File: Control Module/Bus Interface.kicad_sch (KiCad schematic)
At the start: 5 parts, among them J2 Conn_01x22, J3 Conn_01x22, U11 74HC08, U12 74HC08, U13 74HC08

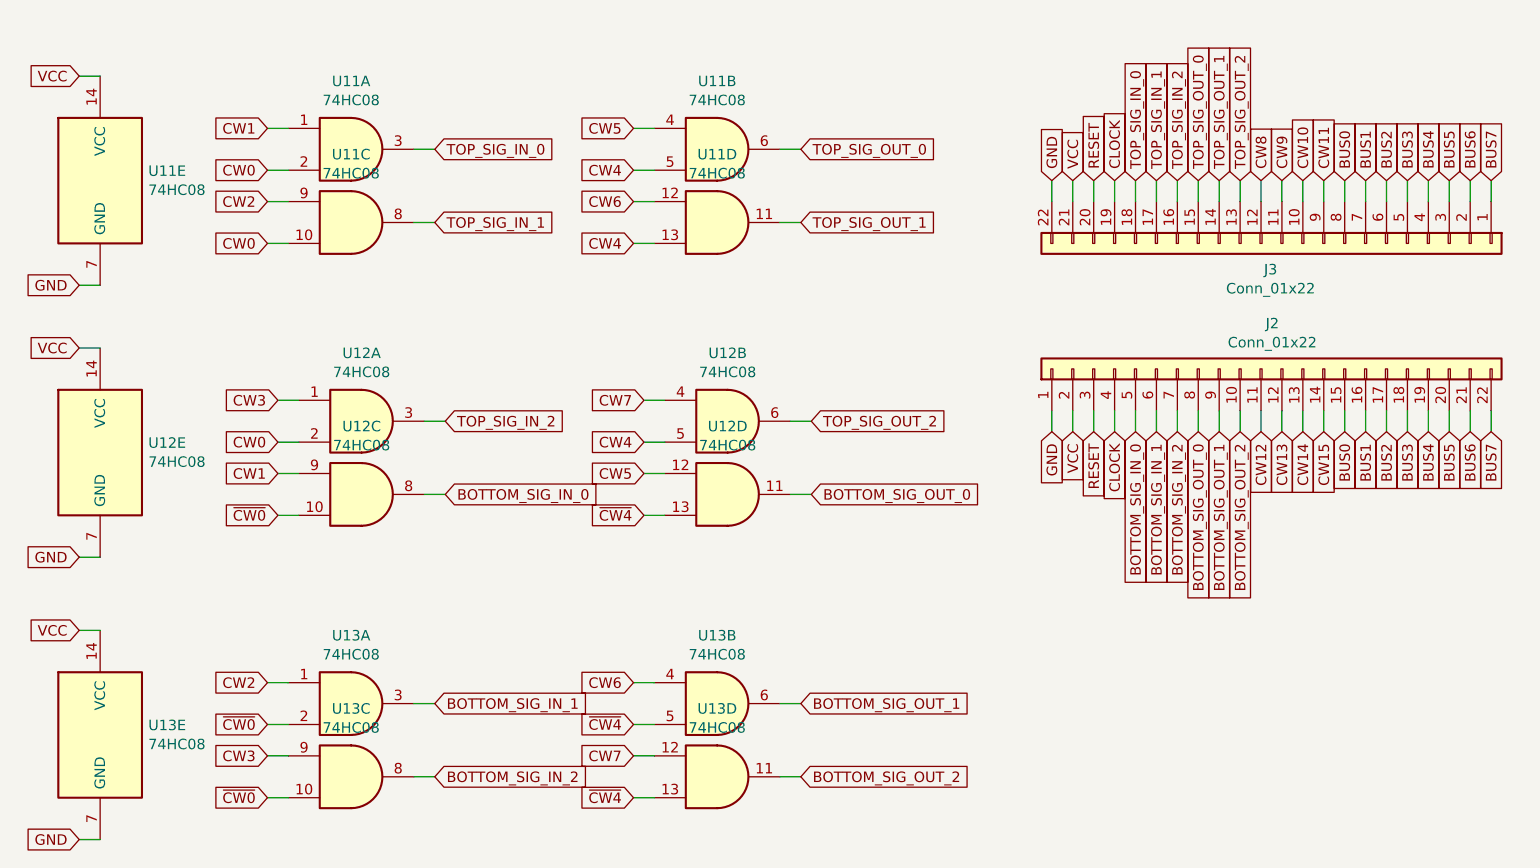
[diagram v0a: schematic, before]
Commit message: Make Control Module 4 layers, and add 2 GND pins per side
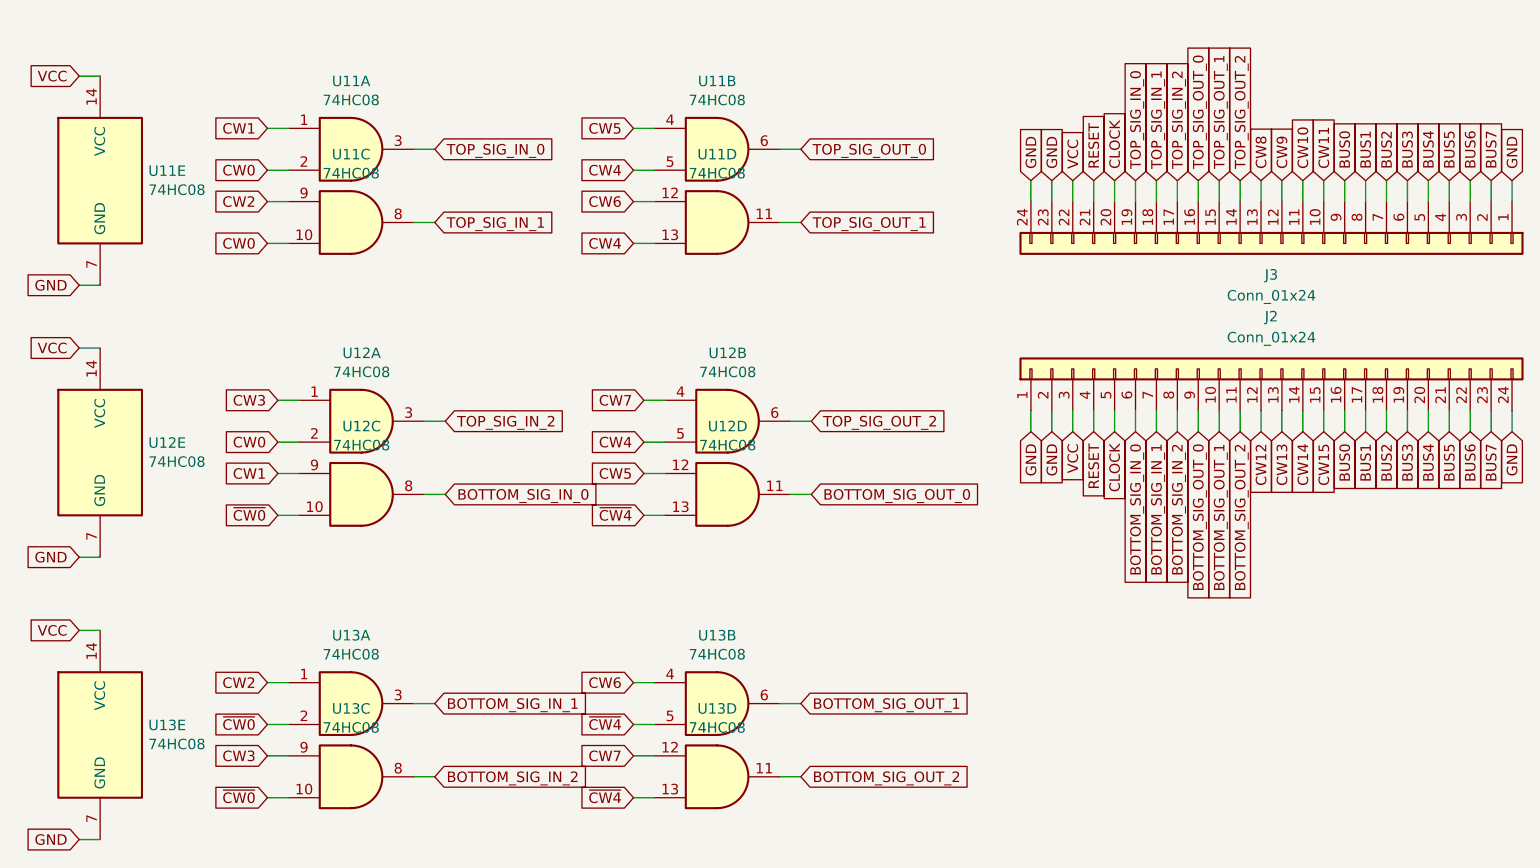
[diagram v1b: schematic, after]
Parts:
- removed J2, J3: Conn_01x22, Connector_PinSocket_2.54mm:PinSocket_1x22_P2.54mm_Horizontal, symbol Connector_Generic:Conn_01x22
- added J2, J3: Conn_01x24, Connector_PinSocket_2.54mm:PinSocket_1x24_P2.54mm_Horizontal, symbol Connector_Generic:Conn_01x24
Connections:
- net BOTTOM_SIG_IN_0: now also J2.6 (Pin_6)
- net BOTTOM_SIG_IN_1: now also J2.7 (Pin_7)
- net BOTTOM_SIG_IN_2: now also J2.8 (Pin_8)
- net BOTTOM_SIG_OUT_0: now also J2.9 (Pin_9)
- net BOTTOM_SIG_OUT_1: now also J2.10 (Pin_10)
- net BOTTOM_SIG_OUT_2: now also J2.11 (Pin_11)
- net BUS0: now also J2.16 (Pin_16), J3.9 (Pin_9)
- net BUS1: now also J2.17 (Pin_17), J3.8 (Pin_8)
- net BUS2: now also J2.18 (Pin_18), J3.7 (Pin_7)
- net BUS3: now also J2.19 (Pin_19), J3.6 (Pin_6)
- net BUS4: now also J2.20 (Pin_20), J3.5 (Pin_5)
- net BUS5: now also J2.21 (Pin_21), J3.4 (Pin_4)
- net BUS6: now also J2.22 (Pin_22), J3.3 (Pin_3)
- net BUS7: now also J2.23 (Pin_23), J3.2 (Pin_2)
- net CLOCK: now also J2.5 (Pin_5), J3.20 (Pin_20)
- net CW10: now also J3.11 (Pin_11)
- net CW11: now also J3.10 (Pin_10)
- net CW12: now also J2.12 (Pin_12)
- net CW13: now also J2.13 (Pin_13)
- net CW14: now also J2.14 (Pin_14)
- net CW15: now also J2.15 (Pin_15)
- net CW8: now also J3.13 (Pin_13)
- net CW9: now also J3.12 (Pin_12)
- net GND: now also J2.1 (Pin_1), J2.2 (Pin_2), J2.24 (Pin_24), J3.1 (Pin_1), J3.23 (Pin_23), J3.24 (Pin_24)
- net RESET: now also J2.4 (Pin_4), J3.21 (Pin_21)
- net TOP_SIG_IN_0: now also J3.19 (Pin_19)
- net TOP_SIG_IN_1: now also J3.18 (Pin_18)
- net TOP_SIG_IN_2: now also J3.17 (Pin_17)
- net TOP_SIG_OUT_0: now also J3.16 (Pin_16)
- net TOP_SIG_OUT_1: now also J3.15 (Pin_15)
- net TOP_SIG_OUT_2: now also J3.14 (Pin_14)
- net VCC: now also J2.3 (Pin_3), J3.22 (Pin_22)
